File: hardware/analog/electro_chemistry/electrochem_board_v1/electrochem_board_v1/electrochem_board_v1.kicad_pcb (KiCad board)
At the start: 2 copper layers, 134.8 x 109.7 mm, 12 parts, among them J1 Conn_01x06_Male, J2 ATX-24, J3 Metallic_Electrode, J4 Metallic_Electrode, Q1 FQP27P06, U1 INA181

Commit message: elchem ctl board
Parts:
- removed J4: Metallic_Electrode, electrodes:Electrode_ThroughHole_V0.1
- added C2: C, Capacitor_SMD:C_0402_1005Metric, F.Cu at (92.3, 136.2)
- added C3: C, Capacitor_SMD:C_0603_1608Metric, F.Cu at (85.9, 136.2)
- added L1: L, Inductor_SMD:L_1210_3225Metric, F.Cu at (86.7, 132.8)
- added R5: R, Resistor_SMD:R_0402_1005Metric, F.Cu at (89.4, 136.2)
- added R6: R, Resistor_SMD:R_0402_1005Metric, F.Cu at (96.4, 131.7)
- added U2: LTC3406ES5, Package_TO_SOT_SMD:TSOT-23-5, F.Cu at (92.2, 132.9)
- J3: value Metallic_Electrode -> Conn_01x02_Male; footprint electrodes:Electrode_ThroughHole_V0.1 -> Connector_Wire:SolderWire-1.5sqmm_1x02_P6mm_D1.7mm_OD3mm
- moved J3 19.8 mm to (148.8, 106.5), turned to 270 degrees
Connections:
- J2 pad 9: Net-(J2-Pad9) -> 5VSB

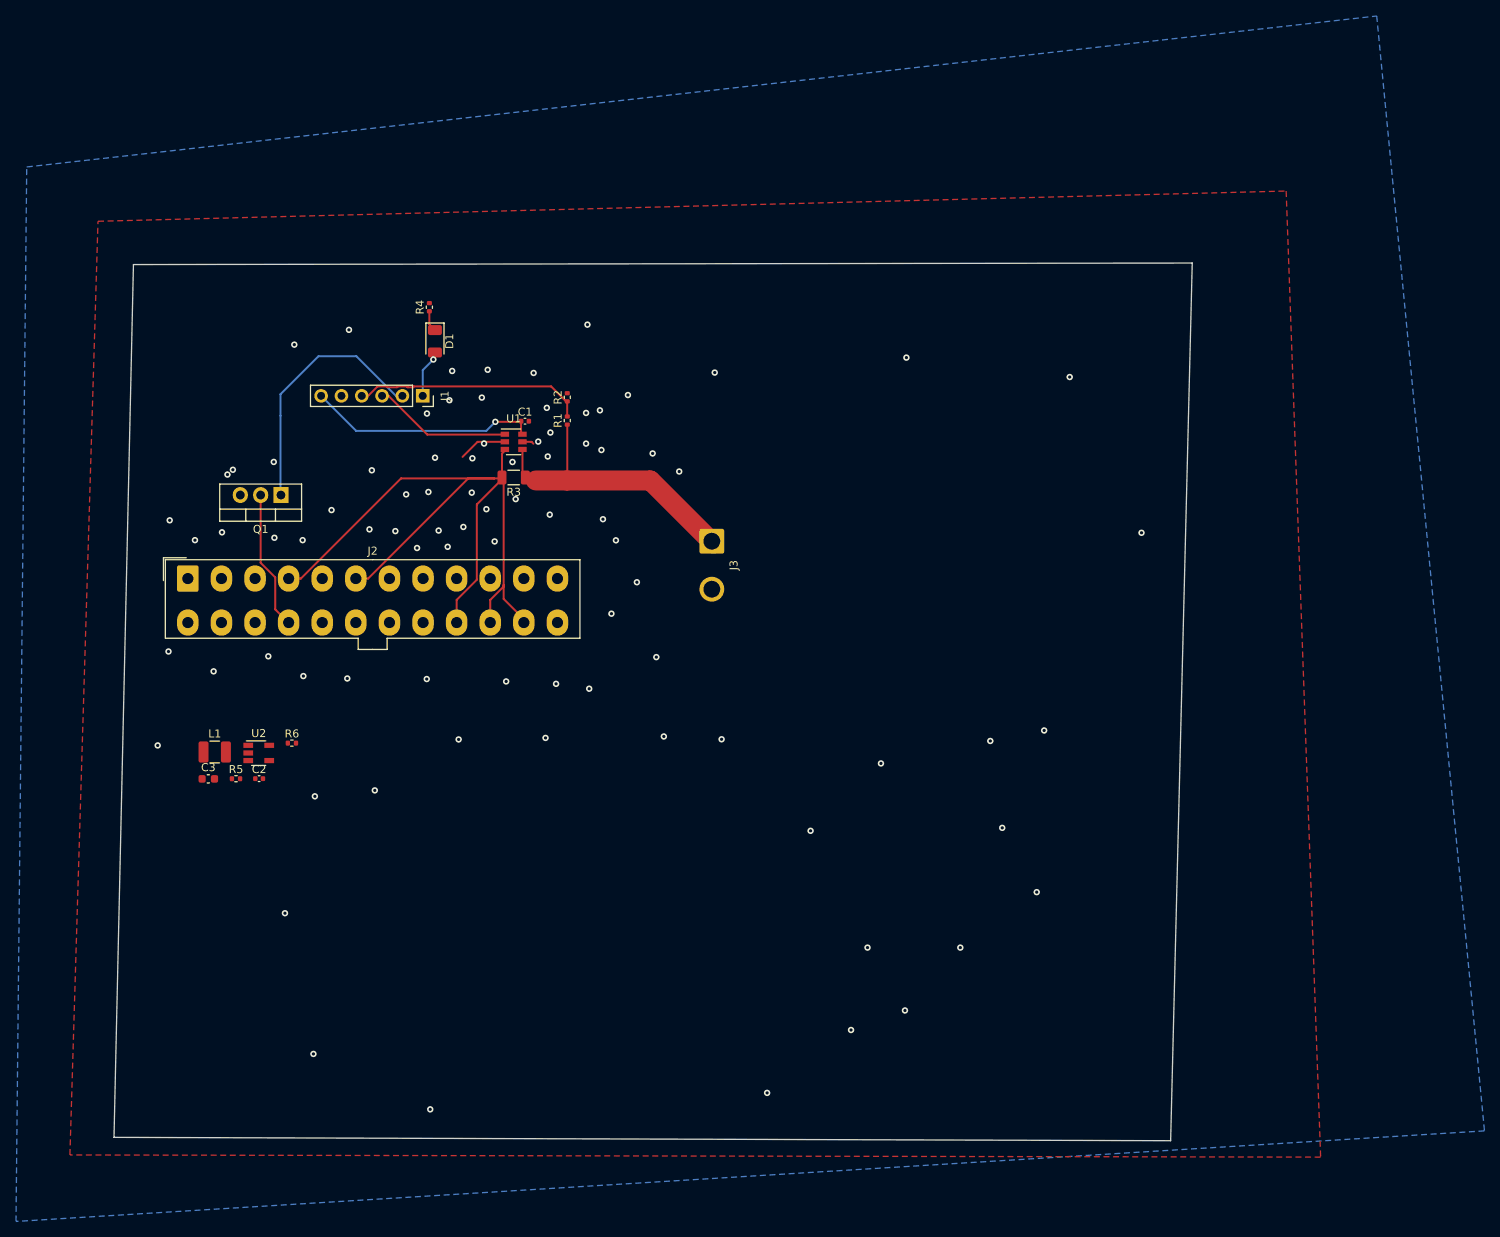
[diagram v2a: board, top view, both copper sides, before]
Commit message: PWM => detect / flyback
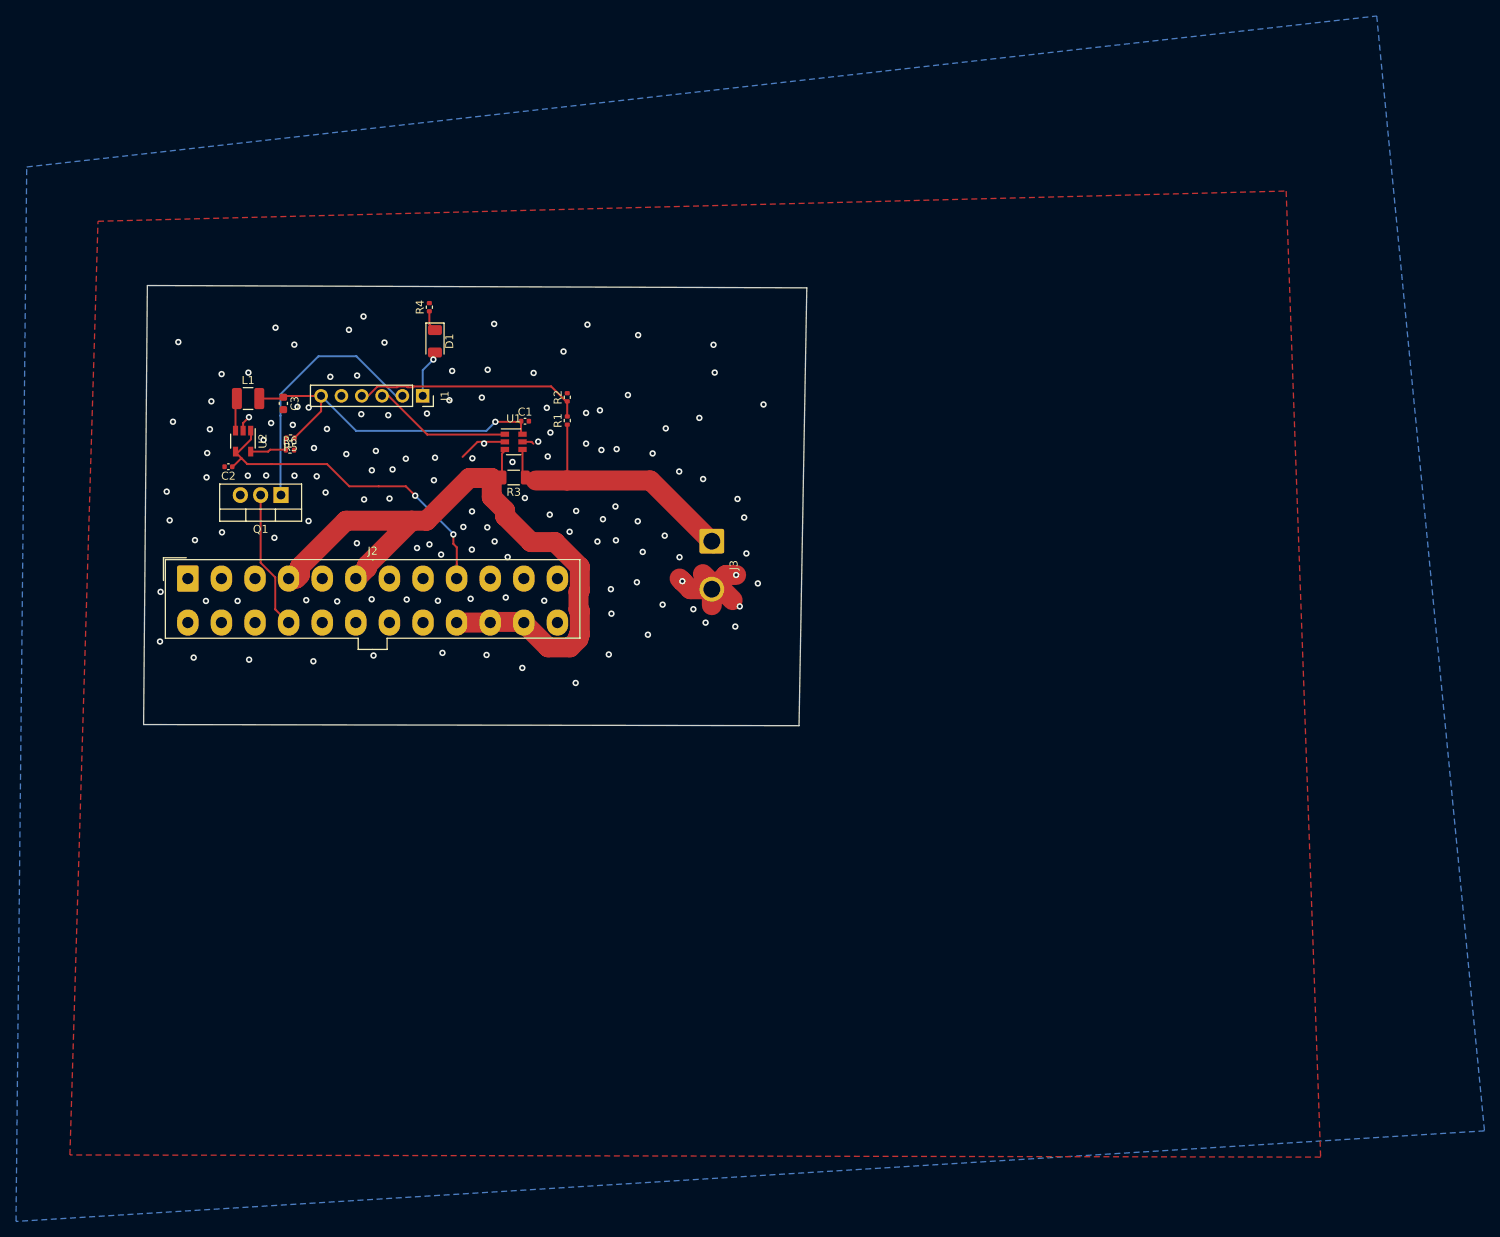
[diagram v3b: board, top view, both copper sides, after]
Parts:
- moved C3 47.9 mm to (95.3, 89.3), turned to 270 degrees
- moved L1 44.4 mm to (90.9, 88.7)
- moved R5 43.1 mm to (96.2, 93.6), turned to 180 degrees
- moved C2 39.2 mm to (88.4, 97.2), turned to 180 degrees
- moved U2 39.0 mm to (90.3, 94.0), turned to 270 degrees
- moved R6 36.6 mm to (96.1, 95.1)
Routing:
- net 5VSB: track 0.00 -> 44.1 mm, vias 0 -> 2
- net GND: track 7.54 -> 26.2 mm, vias 86 -> 134
- net +3V3: track 28.9 -> 43.2 mm
- net 5VPSU: track 101.5 -> 92.5 mm
- net Net-(R5-Pad2): track 0.00 -> 5.92 mm
- net Net-(L1-Pad1): track 0.00 -> 3.91 mm
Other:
- board size 134.8 x 109.7 mm -> 82.9 x 55 mm
- net class power added: clearance 0.2, trace_width 2.5, via_dia 0.8, via_drill 0.4
